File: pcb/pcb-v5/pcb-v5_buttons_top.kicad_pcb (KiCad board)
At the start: 2 copper layers, 14 parts, among them J1 Conn_01x05_Female, J2 Conn_01x05_Female, J3 Conn_01x05_Female, J4 Conn_01x05_Male, SW1 G71Y, SW2 G71Y, SW3 G71Y, U1 AMS1117-3.3

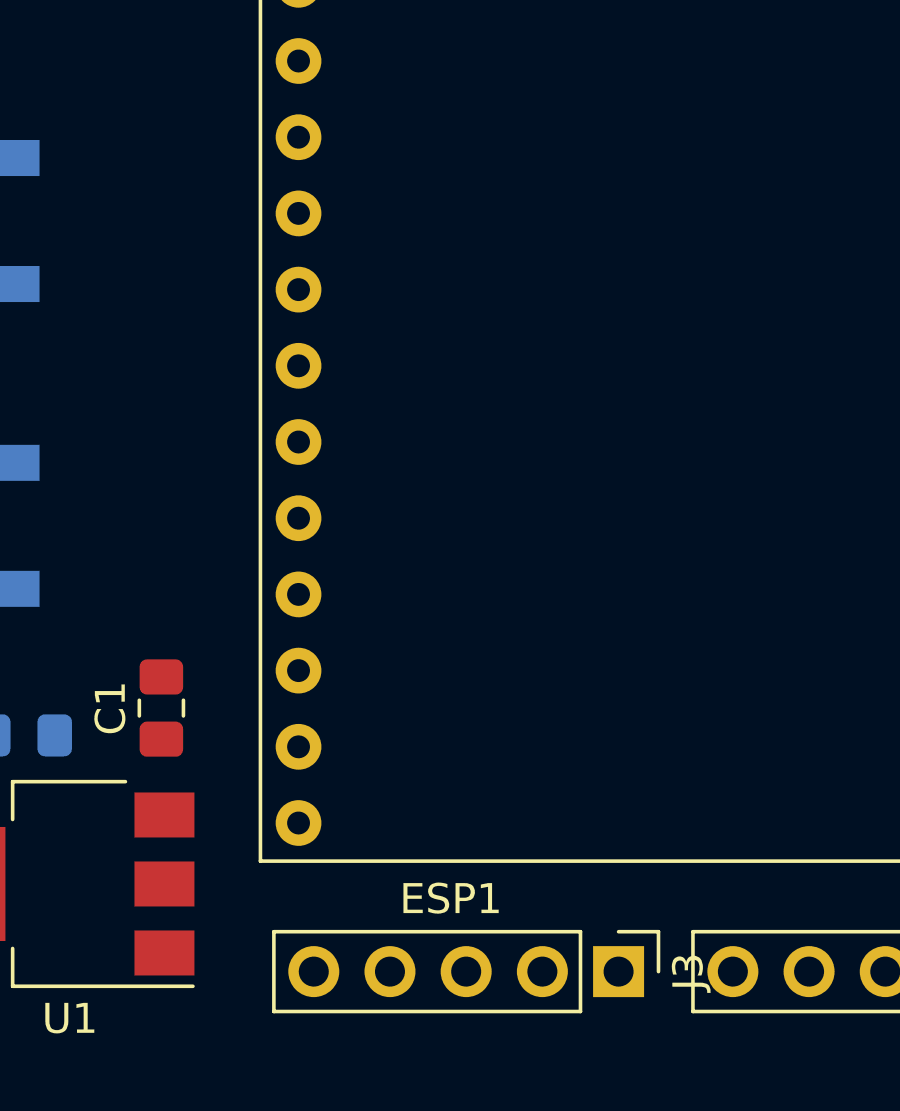
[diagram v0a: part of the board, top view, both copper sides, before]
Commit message: PCB-V2 update
Added OSHW logo on both boards.
Upgraded power lines size to 0.6604.
Added every needed screen printings (VCC,SDA,SCL,...)
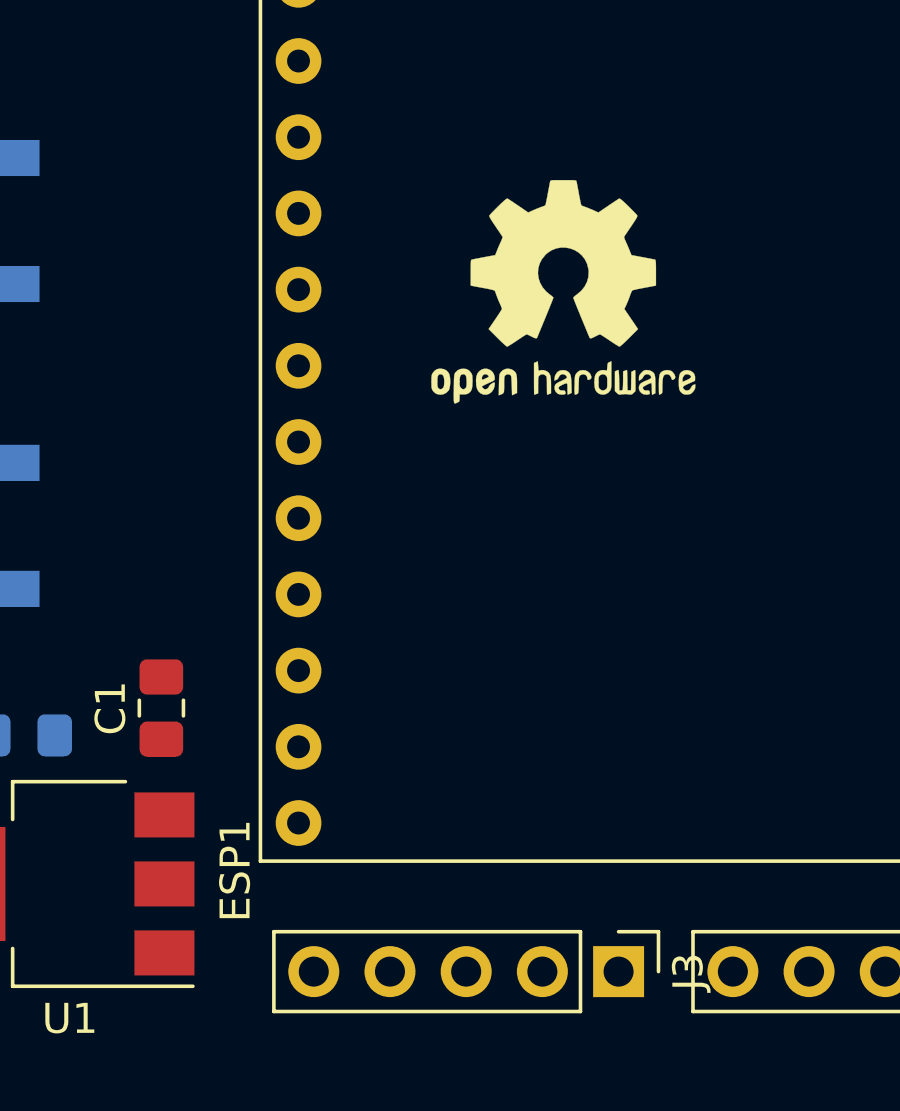
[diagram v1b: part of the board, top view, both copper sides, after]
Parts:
- added REF**: OSHW-Logo2_9.8x8mm_SilkScreen, Symbol:OSHW-Logo2_9.8x8mm_SilkScreen, F.Cu at (148.5, 86.4)
